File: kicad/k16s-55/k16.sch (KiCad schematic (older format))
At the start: 352 parts, among them J1 PCIEPWR, J3 PINHD-1X4, J5 PINHD-1X4, Q1 NDS351AN, U1 AVALON255, U10 AVALON255, U11 AVALON255, U12 AVALON255, U13 AVALON255, U14 AVALON255, U15 AVALON255, U16 AVALON255, U17 PIC16LF1459, U18 IR3895, U19 IR3895, U2 AVALON255, U20 MCP16321, U21 NL27WZ14, U22 NCP694, U23 NCP694, U24 74AUP2G02, U25 NL27WZ14, U3 AVALON255, U4 AVALON255, U5 AVALON255, U6 AVALON255, U7 AVALON255, U8 AVALON255, U9 AVALON255, X1 ASMDB

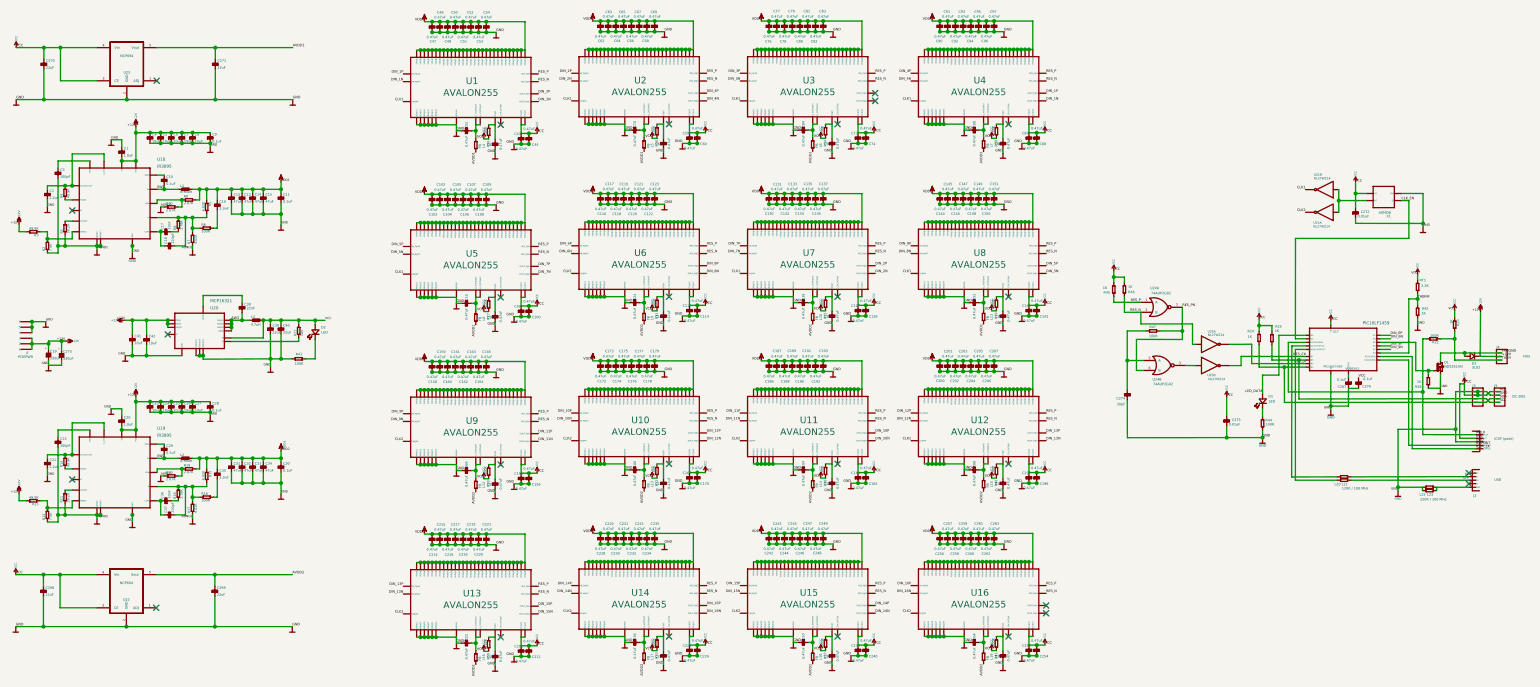
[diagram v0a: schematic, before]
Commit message: Fixing stuff in K16-55
Netlists, versions, names of the sheets, descriptions, component values,
library
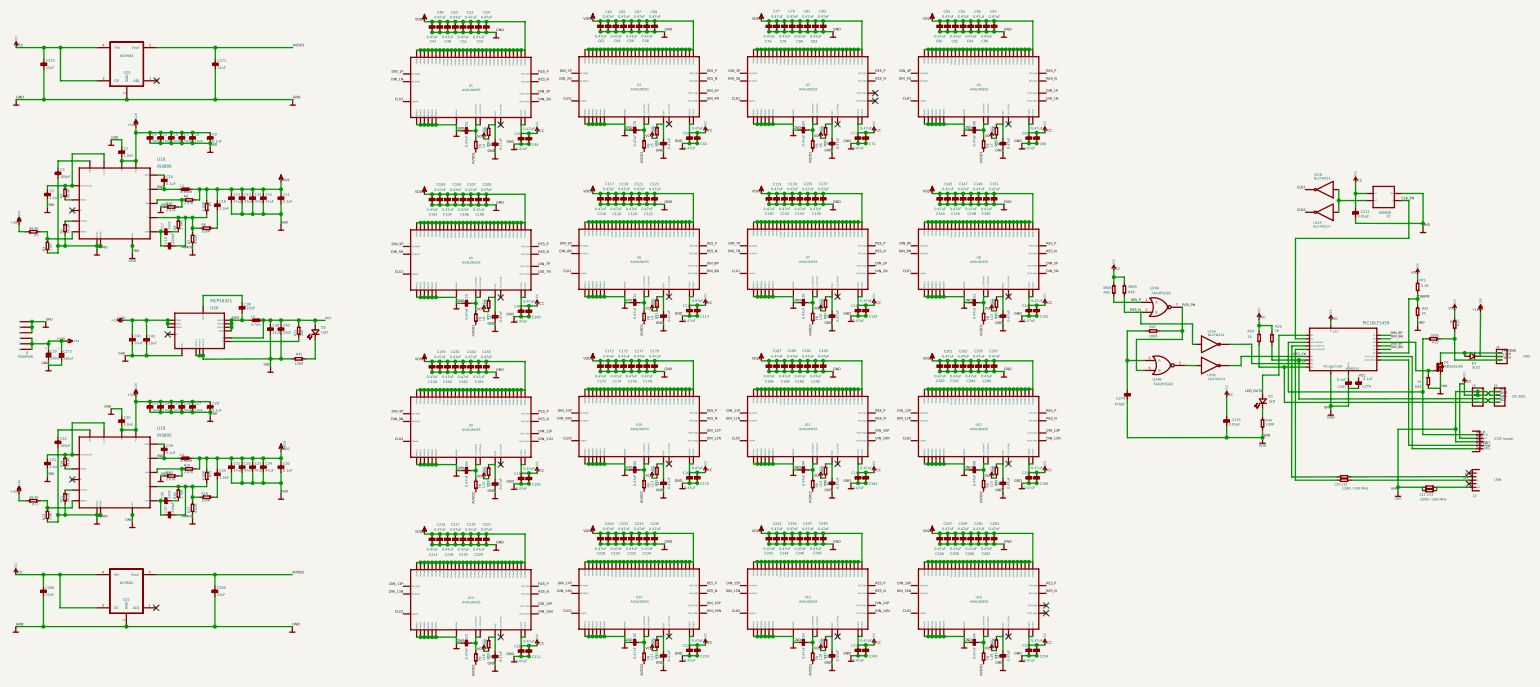
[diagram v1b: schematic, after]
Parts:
- C274: value 30pF -> 470pF
- R45, R46: value 1K -> 390R
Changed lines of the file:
@@
-EESchema Schematic File Version 2  date 30. 11. 2013 14:34:21
+EESchema Schematic File Version 2  date 25. 12. 2013 0:12:21
 LIBS:k16
 LIBS:power
@@
 encoding utf-8
 Sheet 1 1
-Title "Klondike 16-55 ASIC Miner (55nm Avalons)"
-Date "30 nov 2013"
-Rev ""
+Title "Klondike 16-55 ASIC Miner"
+Date "24 dec 2013"
+Rev "1.0.1"
 Comp ""
-Comment1 ""
+Comment1 "For 55nm Avalons - A255"
 Comment2 ""
 Comment3 ""
@@
 P 11857 6443
 F 0 "C274" H 11877 6447 22  0000 L BNN
-F 1 "30pF" H 11878 6499 22  0000 L BNN
+F 1 "470pF" H 11878 6499 22  0000 L BNN
 F 2 "" H 11857 6443 60  0001 C CNN
 F 3 "" H 11857 6443 60  0001 C CNN
@@
 P 11735 5475
 F 0 "R45" V 11775 5382 22  0000 L BNN
-F 1 "1K" V 11733 5376 22  0000 L BNN
+F 1 "390R" V 11733 5376 22  0000 L BNN
 F 2 "" H 11735 5475 60  0001 C CNN
 F 3 "" H 11735 5475 60  0001 C CNN
@@
 P 11831 5474
 F 0 "R46" V 11868 5508 22  0000 L BNN
-F 1 "1K" V 11820 5507 22  0000 L BNN
+F 1 "390R" V 11820 5507 22  0000 L BNN
 F 2 "" H 11831 5474 60  0001 C CNN
 F 3 "" H 11831 5474 60  0001 C CNN
@@
 U 1 1 5294E0F7
 P 5922 3696
-F 0 "U1" H 5933 3802 60  0000 C CNN
-F 1 "AVALON255" H 5922 3696 60  0000 C CNN
+F 0 "U1" H 5922 3761 20  0000 C CNN
+F 1 "AVALON255" H 5927 3721 20  0000 C CNN
 F 2 "~" H 5922 3696 60  0000 C CNN
 F 3 "~" H 5922 3696 60  0000 C CNN
@@
 U 1 1 5295B959
 P 7444 3690
-F 0 "U2" H 7455 3796 60  0000 C CNN
-F 1 "AVALON255" H 7444 3690 60  0000 C CNN
+F 0 "U2" H 7444 3755 20  0000 C CNN
+F 1 "AVALON255" H 7449 3715 20  0000 C CNN
 F 2 "~" H 7444 3690 60  0000 C CNN
 F 3 "~" H 7444 3690 60  0000 C CNN
@@
 U 1 1 5295BC5B
 P 8968 3690
-F 0 "U3" H 8979 3796 60  0000 C CNN
-F 1 "AVALON255" H 8968 3690 60  0000 C CNN
+F 0 "U3" H 8968 3755 20  0000 C CNN
+F 1 "AVALON255" H 8973 3715 20  0000 C CNN
 F 2 "~" H 8968 3690 60  0000 C CNN
 F 3 "~" H 8968 3690 60  0000 C CNN
@@
 U 1 1 5295BD38
 P 10513 3690
-F 0 "U4" H 10524 3796 60  0000 C CNN
-F 1 "AVALON255" H 10513 3690 60  0000 C CNN
+F 0 "U4" H 10513 3755 20  0000 C CNN
+F 1 "AVALON255" H 10518 3715 20  0000 C CNN
 F 2 "~" H 10513 3690 60  0000 C CNN
 F 3 "~" H 10513 3690 60  0000 C CNN
@@
 U 1 1 5295BE17
 P 5922 5256
-F 0 "U5" H 5933 5362 60  0000 C CNN
-F 1 "AVALON255" H 5922 5256 60  0000 C CNN
+F 0 "U5" H 5922 5321 20  0000 C CNN
+F 1 "AVALON255" H 5927 5281 20  0000 C CNN
 F 2 "~" H 5922 5256 60  0000 C CNN
 F 3 "~" H 5922 5256 60  0000 C CNN
@@
 U 1 1 5295BEF0
 P 7444 5250
-F 0 "U6" H 7455 5356 60  0000 C CNN
-F 1 "AVALON255" H 7444 5250 60  0000 C CNN
+F 0 "U6" H 7444 5315 20  0000 C CNN
+F 1 "AVALON255" H 7449 5275 20  0000 C CNN
 F 2 "~" H 7444 5250 60  0000 C CNN
 F 3 "~" H 7444 5250 60  0000 C CNN
@@
 U 1 1 5295BFC9
 P 8968 5250
-F 0 "U7" H 8979 5356 60  0000 C CNN
-F 1 "AVALON255" H 8968 5250 60  0000 C CNN
+F 0 "U7" H 8968 5315 20  0000 C CNN
+F 1 "AVALON255" H 8973 5275 20  0000 C CNN
 F 2 "~" H 8968 5250 60  0000 C CNN
 F 3 "~" H 8968 5250 60  0000 C CNN
@@
 U 1 1 5295C0A2
 P 10513 5250
-F 0 "U8" H 10524 5356 60  0000 C CNN
-F 1 "AVALON255" H 10513 5250 60  0000 C CNN
+F 0 "U8" H 10513 5315 20  0000 C CNN
+F 1 "AVALON255" H 10518 5275 20  0000 C CNN
 F 2 "~" H 10513 5250 60  0000 C CNN
 F 3 "~" H 10513 5250 60  0000 C CNN
@@
 U 1 1 5295C18D
 P 5922 6768
-F 0 "U9" H 5933 6874 60  0000 C CNN
-F 1 "AVALON255" H 5922 6768 60  0000 C CNN
+F 0 "U9" H 5922 6833 20  0000 C CNN
+F 1 "AVALON255" H 5927 6793 20  0000 C CNN
 F 2 "~" H 5922 6768 60  0000 C CNN
 F 3 "~" H 5922 6768 60  0000 C CNN
@@
 U 1 1 5295C266
 P 7444 6762
-F 0 "U10" H 7455 6868 60  0000 C CNN
-F 1 "AVALON255" H 7444 6762 60  0000 C CNN
+F 0 "U10" H 7444 6827 20  0000 C CNN
+F 1 "AVALON255" H 7449 6787 20  0000 C CNN
 F 2 "~" H 7444 6762 60  0000 C CNN
 F 3 "~" H 7444 6762 60  0000 C CNN
@@
 U 1 1 5295C33F
 P 8968 6762
-F 0 "U11" H 8979 6868 60  0000 C CNN
-F 1 "AVALON255" H 8968 6762 60  0000 C CNN
+F 0 "U11" H 8968 6827 20  0000 C CNN
+F 1 "AVALON255" H 8973 6787 20  0000 C CNN
 F 2 "~" H 8968 6762 60  0000 C CNN
 F 3 "~" H 8968 6762 60  0000 C CNN
@@
 U 1 1 5295C418
 P 10513 6762
-F 0 "U12" H 10524 6868 60  0000 C CNN
-F 1 "AVALON255" H 10513 6762 60  0000 C CNN
+F 0 "U12" H 10513 6827 20  0000 C CNN
+F 1 "AVALON255" H 10518 6787 20  0000 C CNN
 F 2 "~" H 10513 6762 60  0000 C CNN
 F 3 "~" H 10513 6762 60  0000 C CNN
@@
 U 1 1 5295C4F1
 P 5922 8328
-F 0 "U13" H 5933 8434 60  0000 C CNN
-F 1 "AVALON255" H 5922 8328 60  0000 C CNN
+F 0 "U13" H 5922 8393 20  0000 C CNN
+F 1 "AVALON255" H 5927 8353 20  0000 C CNN
 F 2 "~" H 5922 8328 60  0000 C CNN
 F 3 "~" H 5922 8328 60  0000 C CNN
@@
 U 1 1 5295C5CA
 P 7444 8322
-F 0 "U14" H 7455 8428 60  0000 C CNN
-F 1 "AVALON255" H 7444 8322 60  0000 C CNN
+F 0 "U14" H 7444 8387 20  0000 C CNN
+F 1 "AVALON255" H 7449 8347 20  0000 C CNN
 F 2 "~" H 7444 8322 60  0000 C CNN
 F 3 "~" H 7444 8322 60  0000 C CNN
@@
 U 1 1 5295C6A3
 P 8968 8322
-F 0 "U15" H 8979 8428 60  0000 C CNN
-F 1 "AVALON255" H 8968 8322 60  0000 C CNN
+F 0 "U15" H 8968 8387 20  0000 C CNN
+F 1 "AVALON255" H 8973 8347 20  0000 C CNN
 F 2 "~" H 8968 8322 60  0000 C CNN
 F 3 "~" H 8968 8322 60  0000 C CNN
@@
 U 1 1 5295C77C
 P 10513 8322
-F 0 "U16" H 10524 8428 60  0000 C CNN
-F 1 "AVALON255" H 10513 8322 60  0000 C CNN
+F 0 "U16" H 10513 8387 20  0000 C CNN
+F 1 "AVALON255" H 10518 8347 20  0000 C CNN
 F 2 "~" H 10513 8322 60  0000 C CNN
 F 3 "~" H 10513 8322 60  0000 C CNN
